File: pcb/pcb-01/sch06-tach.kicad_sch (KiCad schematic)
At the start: 38 parts, among them Q3 2N7002, U4 TPS7A1601DGN, U8 LM2907M-14, U9 TLV1701DBV

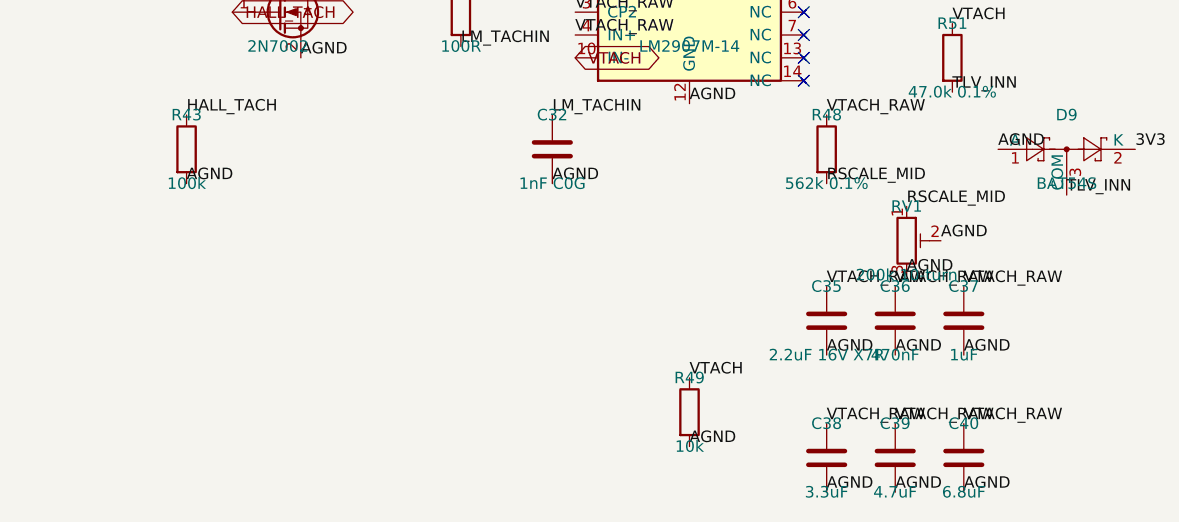
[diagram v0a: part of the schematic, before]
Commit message: pcb: review round 1 fixes — hall pull-up, ground tie, DNP marks, footprints
13-lens board-truth review (netlist as source of truth, spec excluded to
avoid circular validation) found and this commit fixes in the schematic:

- R43 was a 100k pulldown to AGND on HALL_TACH; the DRV5033 is open-drain,
  so the hall line could never go high and the analog overspeed chain could
  never trip. Now 10k pull-up to 3V3 (matching the daughterboard section's
  original intent; the LM2907 spec section contradicted it).
- PGND and AGND had no bridge anywhere (the "wide net tie" was layout-note
  prose only): added NT1 (NetTie-2_SMD_Pad2.0mm) on SCH-03.
- C36-C40 tach filter alternates carried no DNP marking; as captured all six
  caps would be assembled in parallel (~18.5uF, ~12s trip lag). Values now
  say DNP.
- J5 footprint was the vertical BM04B while the BOM ordered the side-entry
  SM04B (mating cable already purchased); footprint corrected.
- U12 TPD2EUSB30 was on SOT-563; the part only exists in DRT 3-pin SOT.
  Now Texas_DRT-3 (stock footprint, cites this exact part).
- R3 PGOOD pull-up moved from VOUT to U3_VCC per TI practice; C17 given a
  rating (22uF 25V X7R).

Spec (docs/electrical.md) updated to match, plus an "Open items from the
2026-07 board-truth review" section for the accepted tradeoffs and firmware
TODOs. bom.csv U12 package corrected. groups.json: C32 reassigned from
dnp_bank to tach (functional filter cap, not an alternate).

ERC: no errors (35 pre-existing same_local_global_label warnings from the
label convention). Board-side sync happens via Update-PCB-from-Schematic.
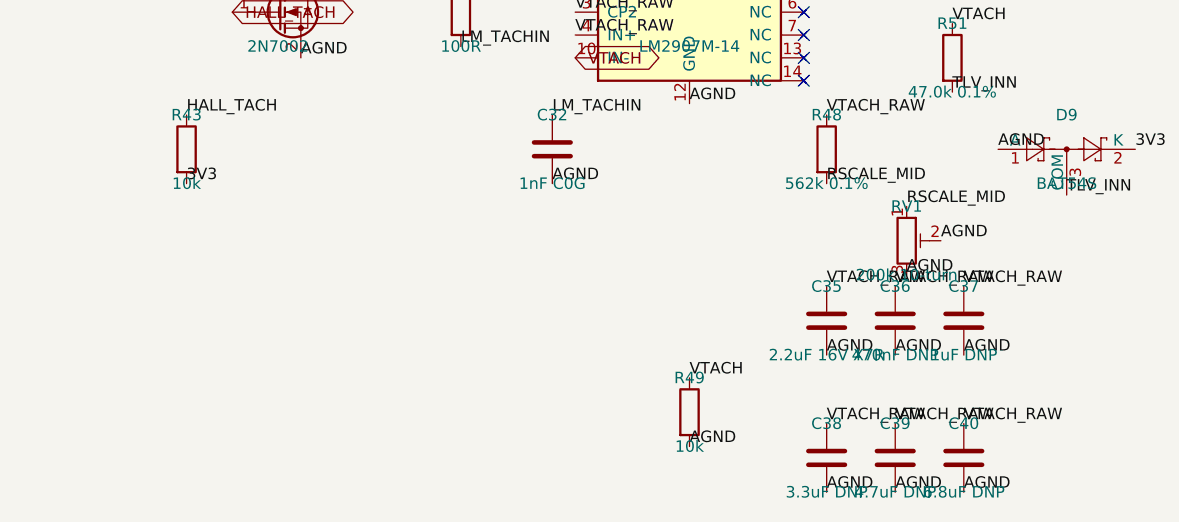
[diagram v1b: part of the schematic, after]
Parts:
- C36: value 470nF -> 470nF DNP
- C37: value 1uF -> 1uF DNP
- C38: value 3.3uF -> 3.3uF DNP
- C39: value 4.7uF -> 4.7uF DNP
- C40: value 6.8uF -> 6.8uF DNP
- R43: value 100k -> 10k
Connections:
- net 3V3: now also R43.2
- net AGND: no longer R43.2
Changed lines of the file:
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@@
-)
-  (label "AGND"
-    (at 124.46 109.22 0)
-    (effects
-      (font
-        (size 1.27 1.27))
-      (justify left bottom))
 )
   (label "AGND"
@@
   (label "TACH_LDO_IN"
     (at 44.45 44.45 0)
+    (effects
+      (font
+        (size 1.27 1.27))
+      (justify left bottom))
+)
+  (label "3V3"
+    (at 124.46 109.22 0)
     (effects
       (font
@@
         (font
           (size 1.27 1.27))))
-    (property "Value" "100k"
+    (property "Value" "10k"
       (at 124.46 109.22 0)
       (effects
@@
         (font
           (size 1.27 1.27))))
-    (property "Value" "470nF"
+    (property "Value" "470nF DNP"
       (at 203.2 128.27 0)
       (effects
@@
         (font
           (size 1.27 1.27))))
-    (property "Value" "1uF"
+    (property "Value" "1uF DNP"
       (at 210.82 128.27 0)
       (effects
@@
         (font
           (size 1.27 1.27))))
-    (property "Value" "3.3uF"
+    (property "Value" "3.3uF DNP"
       (at 195.58 143.51 0)
       (effects
@@
         (font
           (size 1.27 1.27))))
-    (property "Value" "4.7uF"
+    (property "Value" "4.7uF DNP"
       (at 203.2 143.51 0)
       (effects
@@
         (font
           (size 1.27 1.27))))
-    (property "Value" "6.8uF"
+    (property "Value" "6.8uF DNP"
       (at 210.82 143.51 0)
       (effects
